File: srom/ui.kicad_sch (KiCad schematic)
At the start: 5 parts, among them J301 Conn_01x05_Female, J302 Conn_01x04_Female, J303 Conn_01x03_Female, U301 Pico-3 UI

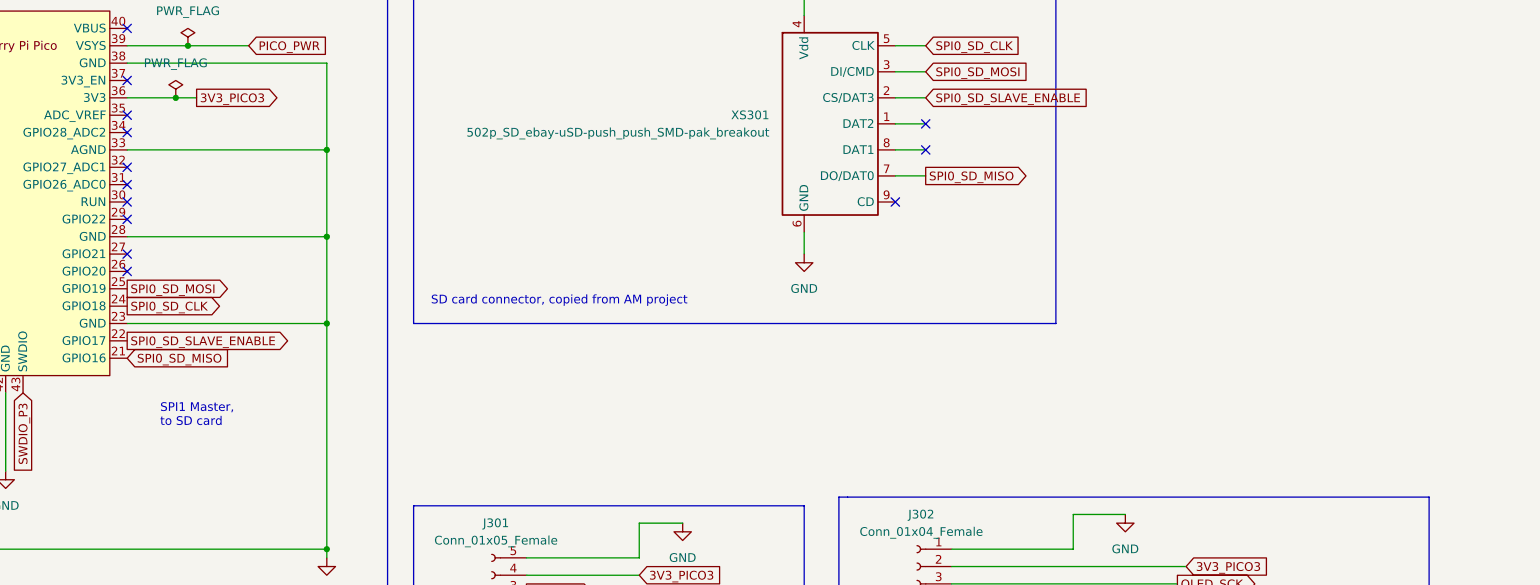
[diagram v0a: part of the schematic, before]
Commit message: add SD card detect to hardware
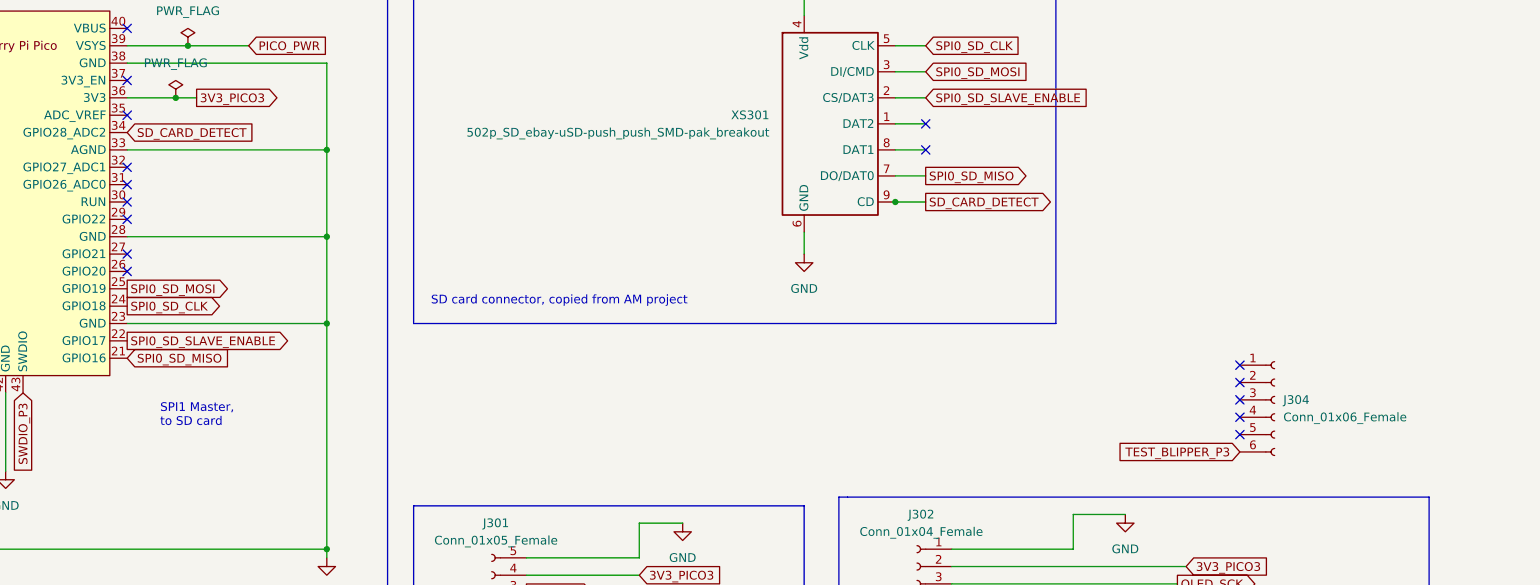
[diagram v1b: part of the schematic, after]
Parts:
- added J304: Conn_01x06_Female, Connector_PinHeader_2.54mm:PinHeader_1x06_P2.54mm_Vertical, symbol Connector:Conn_01x06_Female
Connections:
- net TEST_BLIPPER_P3: now also J304.6 (Pin_6)
- net SD_CARD_DETECT: now reaches XS301.9 (CD)
- net SD_CARD_DETECT: now also U301.34 (GPIO28_ADC2)
- no-connect marks 19 -> 22
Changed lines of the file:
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@@
   (junction (at 119.38 78.74) (diameter 0) (color 0 0 0 0)
   )
+  (junction (at 202.565 60.96) (diameter 0) (color 0 0 0 0)
+  )
   (junction (at 119.38 53.34) (diameter 0) (color 0 0 0 0)
   )
@@
   (junction (at 30.48 66.04) (diameter 0) (color 0 0 0 0)
   )
+  (no_connect (at 252.984 92.456))
   (no_connect (at 207.01 49.53))
   (no_connect (at 54.61 35.56))
   (no_connect (at 54.61 71.12))
   (no_connect (at 54.61 45.72))
+  (no_connect (at 252.984 84.836))
   (no_connect (at 54.61 38.1))
+  (no_connect (at 252.984 87.376))
   (no_connect (at 54.61 63.5))
   (no_connect (at 90.17 55.88))
   (no_connect (at 90.17 48.26))
+  (no_connect (at 252.984 94.996))
   (no_connect (at 90.17 43.18))
   (no_connect (at 90.17 68.58))
@@
   (no_connect (at 90.17 71.12))
   (no_connect (at 207.01 53.34))
+  (no_connect (at 252.984 89.916))
   (no_connect (at 90.17 35.56))
   (no_connect (at 90.17 58.42))
   (no_connect (at 90.17 63.5))
-  (no_connect (at 202.565 60.96))
-  (no_connect (at 90.17 50.8))
   (wire (pts (xy 30.48 78.74) (xy 54.61 78.74))
     (stroke (width 0) (type default) (color 0 0 0 0))
@@
     (stroke (width 0) (type default) (color 0 0 0 0))
   )
+  (wire (pts (xy 202.438 60.96) (xy 202.565 60.96))
+    (stroke (width 0) (type default) (color 0 0 0 0))
+  )
   (polyline (pts (xy 280.67 104.14) (xy 280.67 132.08))
     (stroke (width 0) (type default) (color 0 0 0 0))
@@
   )
   (wire (pts (xy 148.59 113.03) (xy 165.1 113.03))
+    (stroke (width 0) (type default) (color 0 0 0 0))
+  )
+  (wire (pts (xy 202.565 60.96) (xy 207.01 60.96))
     (stroke (width 0) (type default) (color 0 0 0 0))
   )
@@
     )
   )
+  (global_label "SD_CARD_DETECT" (shape output) (at 207.01 60.96 0) (fields_autoplaced)
+    (effects (font (size 1.27 1.27)) (justify left))
+    (property "Intersheet References" "${INTERSHEET_REFS}" (id 0) (at 225.5098 60.8806 0)
+      (effects (font (size 1.27 1.27)) (justify left) hide)
+    )
+  )
   (global_label "OLED_SDA" (shape output) (at 243.84 119.38 0) (fields_autoplaced)
     (effects (font (size 1.27 1.27)) (justify left))
@@
     )
   )
+  (global_label "SD_CARD_DETECT" (shape input) (at 90.17 50.8 0) (fields_autoplaced)
+    (effects (font (size 1.27 1.27)) (justify left))
+    (property "Intersheet References" "${INTERSHEET_REFS}" (id 0) (at 108.6698 50.7206 0)
+      (effects (font (size 1.27 1.27)) (justify left) hide)
+    )
+  )
   (global_label "SPI1_UI_SLAVE_ENABLE" (shape output) (at 54.61 76.2 180) (fields_autoplaced)
     (effects (font (size 1.27 1.27)) (justify right))
@@
     (property "Intersheet References" "${INTERSHEET_REFS}" (id 0) (at 119.7974 38.0206 0)
       (effects (font (size 1.27 1.27)) (justify left) hide)
+    )
+  )
+  (global_label "TEST_BLIPPER_P3" (shape input) (at 252.984 97.536 180) (fields_autoplaced)
+    (effects (font (size 1.27 1.27)) (justify right))
+    (property "Intersheet References" "${INTERSHEET_REFS}" (id 0) (at 234.0004 97.4566 0)
+      (effects (font (size 1.27 1.27)) (justify right) hide)
     )
   )
@@
     (pin "1")
   )
+  (symbol (lib_id "Connector:Conn_01x06_Female") (at 258.064 89.916 0) (unit 1)
+    (in_bom yes) (on_board yes) (fields_autoplaced)
+    (property "Reference" "J304" (id 0) (at 259.334 89.9159 0)
+      (effects (font (size 1.27 1.27)) (justify left))
+    )
+    (property "Value" "Conn_01x06_Female" (id 1) (at 259.334 92.4559 0)
+      (effects (font (size 1.27 1.27)) (justify left))
+    )
+    (property "Footprint" "Connector_PinHeader_2.54mm:PinHeader_1x06_P2.54mm_Vertical" (id 2) (at 258.064 89.916 0)
+      (effects (font (size 1.27 1.27)) hide)
+    )
+    (property "Datasheet" "~" (id 3) (at 258.064 89.916 0)
+      (effects (font (size 1.27 1.27)) hide)
+    )
+    (pin "1")
+    (pin "2")
+    (pin "3")
+    (pin "4")
+    (pin "5")
+    (pin "6")
+  )
   (symbol (lib_id "pico-sym:Pico") (at 72.39 59.69 0) (unit 1)

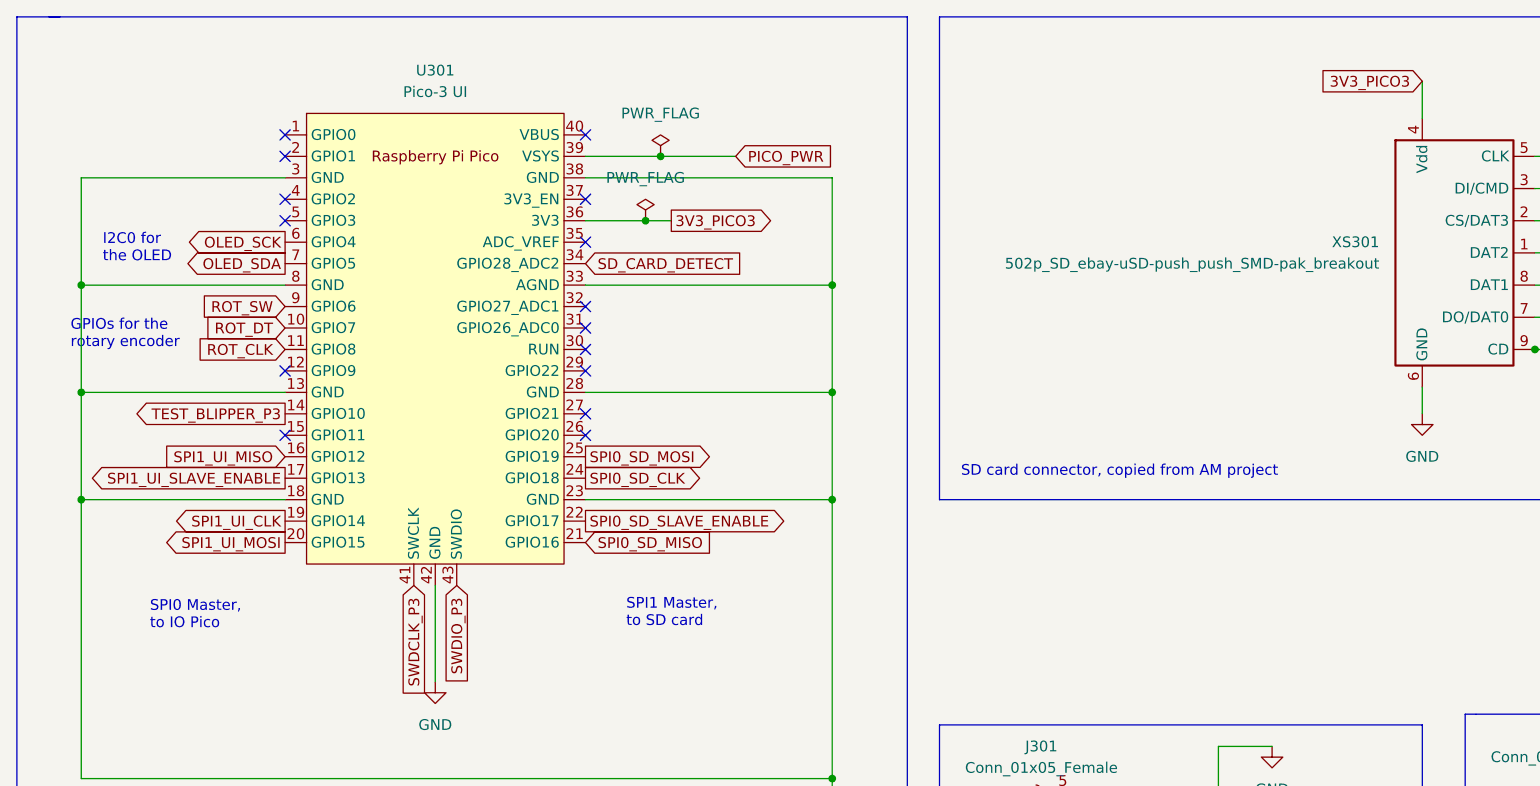
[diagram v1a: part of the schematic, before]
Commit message: update schematic to match UART comms and SD card detect
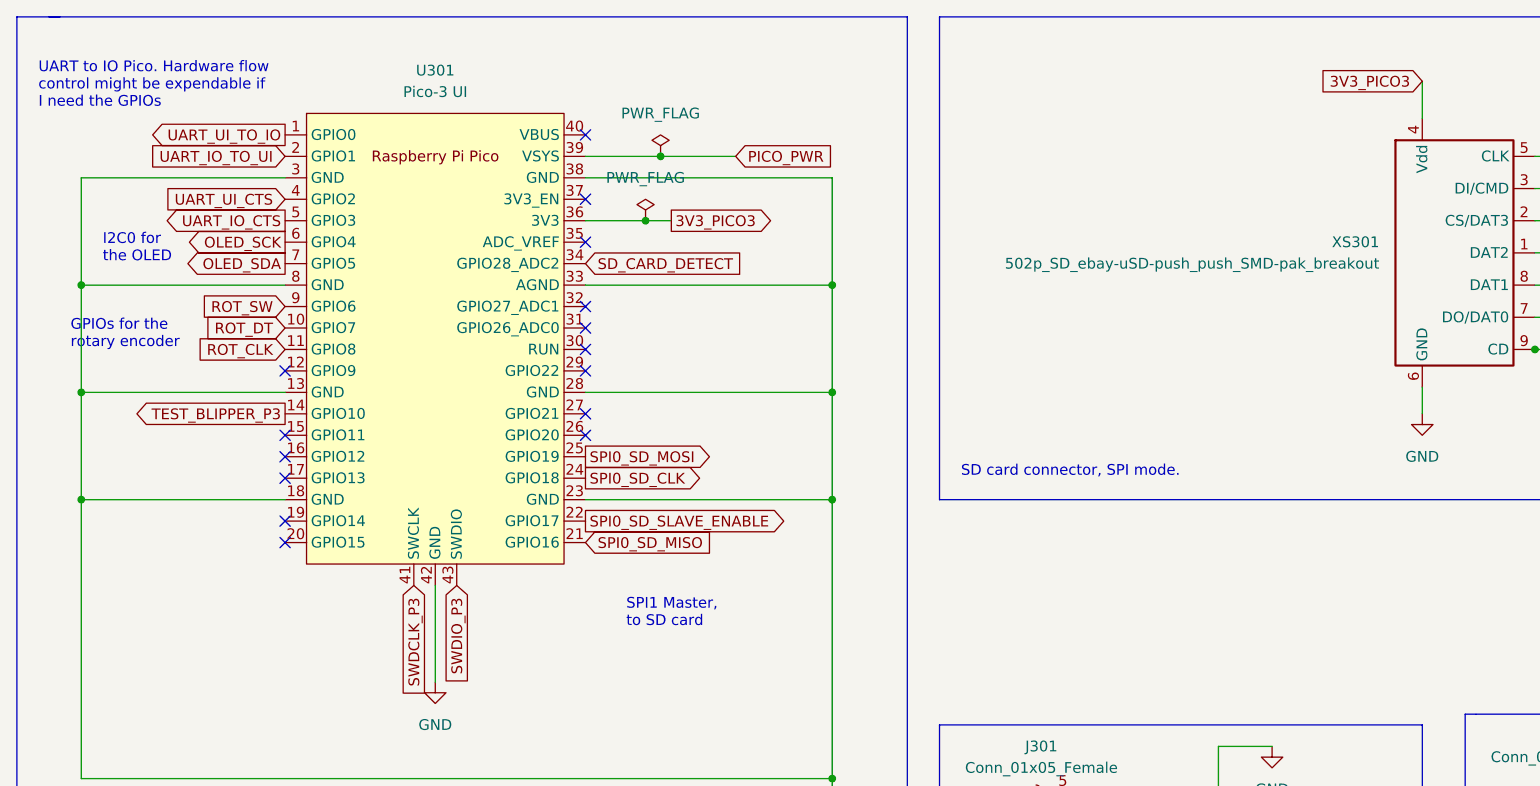
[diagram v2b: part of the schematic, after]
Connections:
- net UART_UI_TO_IO: now reaches U301.1 (GPIO0)
- net UART_IO_TO_UI: now reaches U301.2 (GPIO1)
- net UART_UI_CTS: now reaches U301.4 (GPIO2)
- net UART_IO_CTS: now reaches U301.5 (GPIO3)
- net SPI1_UI_CLK: no longer names the net of U301.19 (GPIO14)
- net SPI1_UI_MISO: no longer names the net of U301.16 (GPIO12)
- net SPI1_UI_MOSI: no longer names the net of U301.20 (GPIO15)
- net SPI1_UI_SLAVE_ENABLE: no longer names the net of U301.17 (GPIO13)
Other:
- note added: "SD card connector, SPI mode."
- note added: "UART to IO Pico. Hardware flow control might be expendable if I need the GPIOs"
- note removed: "SD card connector, copied from AM project"
- note removed: "SPI0 Master, to IO Pico"
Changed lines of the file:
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@@
   (no_connect (at 252.984 92.456))
   (no_connect (at 207.01 49.53))
-  (no_connect (at 54.61 35.56))
+  (no_connect (at 54.61 73.66))
   (no_connect (at 54.61 71.12))
-  (no_connect (at 54.61 45.72))
   (no_connect (at 252.984 84.836))
-  (no_connect (at 54.61 38.1))
   (no_connect (at 252.984 87.376))
   (no_connect (at 54.61 63.5))
   (no_connect (at 90.17 55.88))
+  (no_connect (at 54.61 81.28))
   (no_connect (at 90.17 48.26))
   (no_connect (at 252.984 94.996))
@@
   (no_connect (at 90.17 68.58))
   (no_connect (at 90.17 60.96))
-  (no_connect (at 54.61 43.18))
   (no_connect (at 90.17 71.12))
+  (no_connect (at 54.61 83.82))
   (no_connect (at 207.01 53.34))
   (no_connect (at 252.984 89.916))
   (no_connect (at 90.17 35.56))
+  (no_connect (at 54.61 76.2))
   (no_connect (at 90.17 58.42))
   (no_connect (at 90.17 63.5))
@@
     (effects (font (size 1.27 1.27)) (justify left bottom))
   )
+  (text "UART to IO Pico. Hardware flow\ncontrol might be expendable if\nI need the GPIOs"
+    (at 25.4 32.512 0)
+    (effects (font (size 1.27 1.27)) (justify left bottom))
+  )
   (text "SPI1 Master,\nto SD card" (at 94.996 93.98 0)
     (effects (font (size 1.27 1.27)) (justify left bottom))
@@
   )
   (text "GPIOs for the\nrotary encoder" (at 29.21 60.96 0)
-    (effects (font (size 1.27 1.27)) (justify left bottom))
-  )
-  (text "SPI0 Master,\nto IO Pico" (at 38.608 94.234 0)
     (effects (font (size 1.27 1.27)) (justify left bottom))
   )
@@
     (effects (font (size 1.27 1.27)) (justify right bottom))
   )
-  (text "SD card connector, copied from AM project" (at 134.62 76.2 0)
+  (text "SD card connector, SPI mode." (at 134.62 76.2 0)
     (effects (font (size 1.27 1.27)) (justify left bottom))
   )
@@
     )
   )
-  (global_label "SPI1_UI_CLK" (shape output) (at 54.61 81.28 180) (fields_autoplaced)
-    (effects (font (size 1.27 1.27)) (justify right))
-    (property "Intersheet References" "${INTERSHEET_REFS}" (id 0) (at 40.4645 81.2006 0)
-      (effects (font (size 1.27 1.27)) (justify right) hide)
-    )
-  )
   (global_label "SPI0_SD_MOSI" (shape input) (at 207.01 41.91 0) (fields_autoplaced)
     (effects (font (size 1.27 1.27)) (justify left))
@@
     )
   )
+  (global_label "UART_UI_CTS" (shape input) (at 54.61 43.18 180) (fields_autoplaced)
+    (effects (font (size 1.27 1.27)) (justify right))
+    (property "Intersheet References" "${INTERSHEET_REFS}" (id 0) (at 40.2226 43.1006 0)
+      (effects (font (size 1.27 1.27)) (justify right) hide)
+    )
+  )
   (global_label "3V3_PICO3" (shape output) (at 100.33 45.72 0) (fields_autoplaced)
     (effects (font (size 1.27 1.27)) (justify left))
@@
     )
   )
-  (global_label "SPI1_UI_MOSI" (shape output) (at 54.61 83.82 180) (fields_autoplaced)
-    (effects (font (size 1.27 1.27)) (justify right))
-    (property "Intersheet References" "${INTERSHEET_REFS}" (id 0) (at 39.4364 83.7406 0)
-      (effects (font (size 1.27 1.27)) (justify right) hide)
-    )
-  )
   (global_label "TEST_BLIPPER_P3" (shape output) (at 54.61 68.58 180) (fields_autoplaced)
     (effects (font (size 1.27 1.27)) (justify right))
@@
     )
   )
-  (global_label "SPI1_UI_SLAVE_ENABLE" (shape output) (at 54.61 76.2 180) (fields_autoplaced)
-    (effects (font (size 1.27 1.27)) (justify right))
-    (property "Intersheet References" "${INTERSHEET_REFS}" (id 0) (at 30.4859 76.1206 0)
-      (effects (font (size 1.27 1.27)) (justify right) hide)
-    )
-  )
   (global_label "3V3_PICO3" (shape input) (at 245.11 114.3 0) (fields_autoplaced)
     (effects (font (size 1.27 1.27)) (justify left))
@@
     )
   )
+  (global_label "UART_UI_TO_IO" (shape output) (at 54.61 35.56 180) (fields_autoplaced)
+    (effects (font (size 1.27 1.27)) (justify right))
+    (property "Intersheet References" "${INTERSHEET_REFS}" (id 0) (at 38.4688 35.4806 0)
+      (effects (font (size 1.27 1.27)) (justify right) hide)
+    )
+  )
+  (global_label "UART_IO_CTS" (shape output) (at 54.61 45.72 180) (fields_autoplaced)
+    (effects (font (size 1.27 1.27)) (justify right))
+    (property "Intersheet References" "${INTERSHEET_REFS}" (id 0) (at 40.2226 45.6406 0)
+      (effects (font (size 1.27 1.27)) (justify right) hide)
+    )
+  )
   (global_label "SWDCLK_P3" (shape input) (at 43.815 153.035 0) (fields_autoplaced)
     (effects (font (size 1.27 1.27)) (justify left))
@@
     )
   )
+  (global_label "UART_IO_TO_UI" (shape input) (at 54.61 38.1 180) (fields_autoplaced)
+    (effects (font (size 1.27 1.27)) (justify right))
+    (property "Intersheet References" "${INTERSHEET_REFS}" (id 0) (at 38.4688 38.0206 0)
+      (effects (font (size 1.27 1.27)) (justify right) hide)
+    )
+  )
   (global_label "SPI0_SD_MOSI" (shape output) (at 90.17 73.66 0) (fields_autoplaced)
     (effects (font (size 1.27 1.27)) (justify left))
@@
       (effects (font (size 1.27 1.27)) (justify right) hide)
     )
-  )
-  (global_label "SPI1_UI_MISO" (shape input) (at 54.61 73.66 180) (fields_autoplaced)
-    (effects (font (size 1.27 1.27)) (justify right))
-    (property "Intersheet References" "${INTERSHEET_REFS}" (id 0) (at 39.4364 73.5806 0)
-      (effects (font (size 1.27 1.27)) (justify right) hide)
-    )
